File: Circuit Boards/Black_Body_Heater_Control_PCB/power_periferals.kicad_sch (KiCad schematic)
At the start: 17 parts, among them Q2 SI2310-TP, U2 INA181A2IDBVR, U3 LMR51420XFDDCR

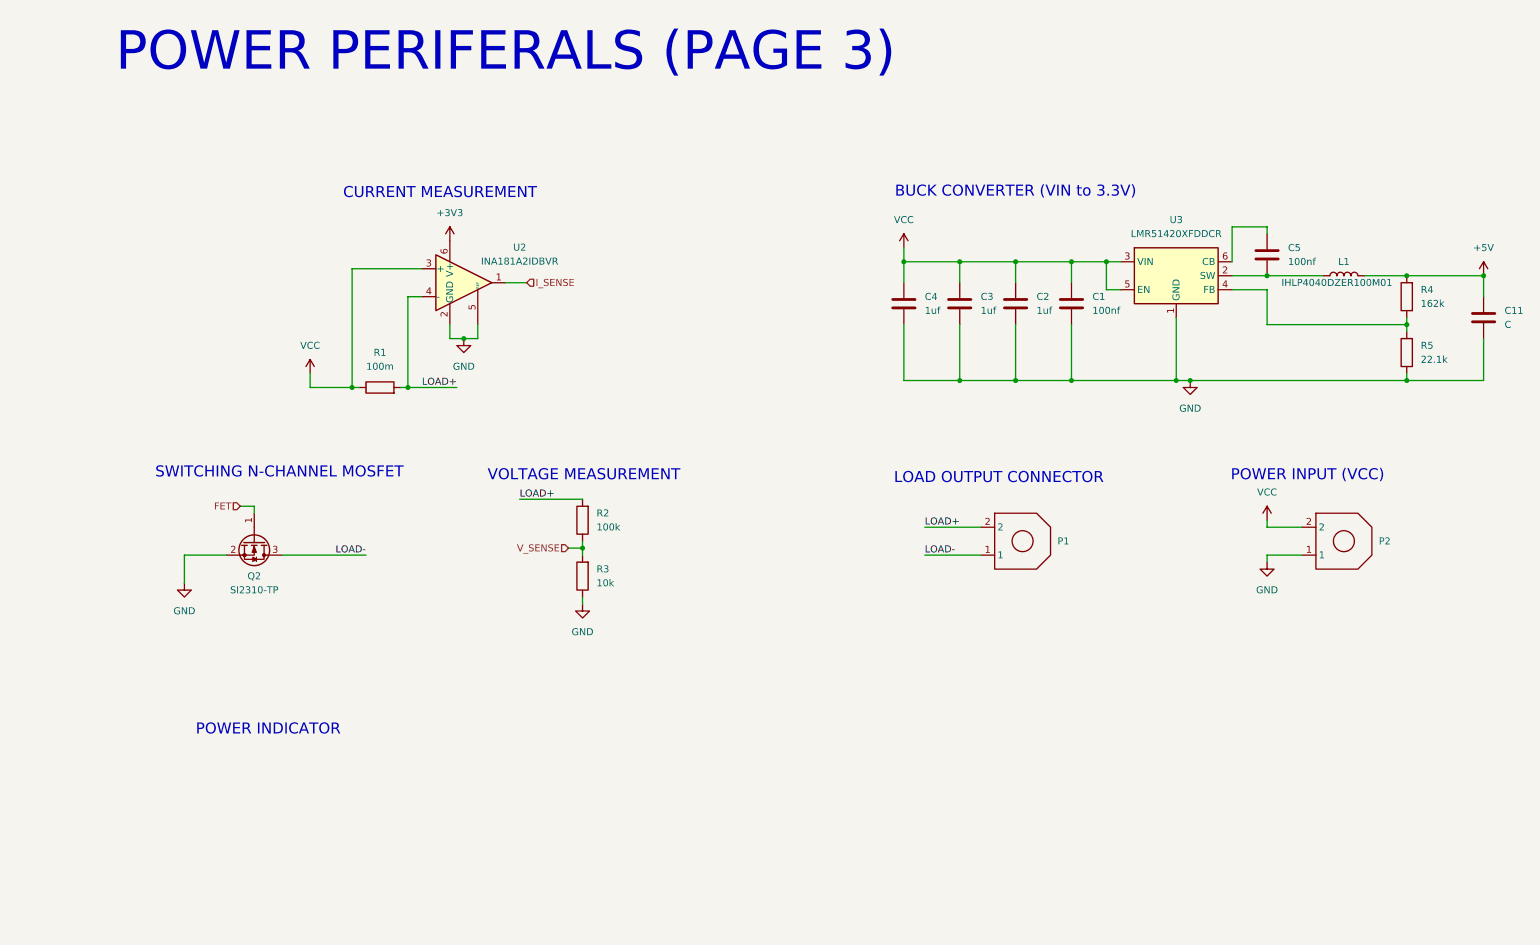
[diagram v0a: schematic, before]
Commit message: Heater PCB done (to review)
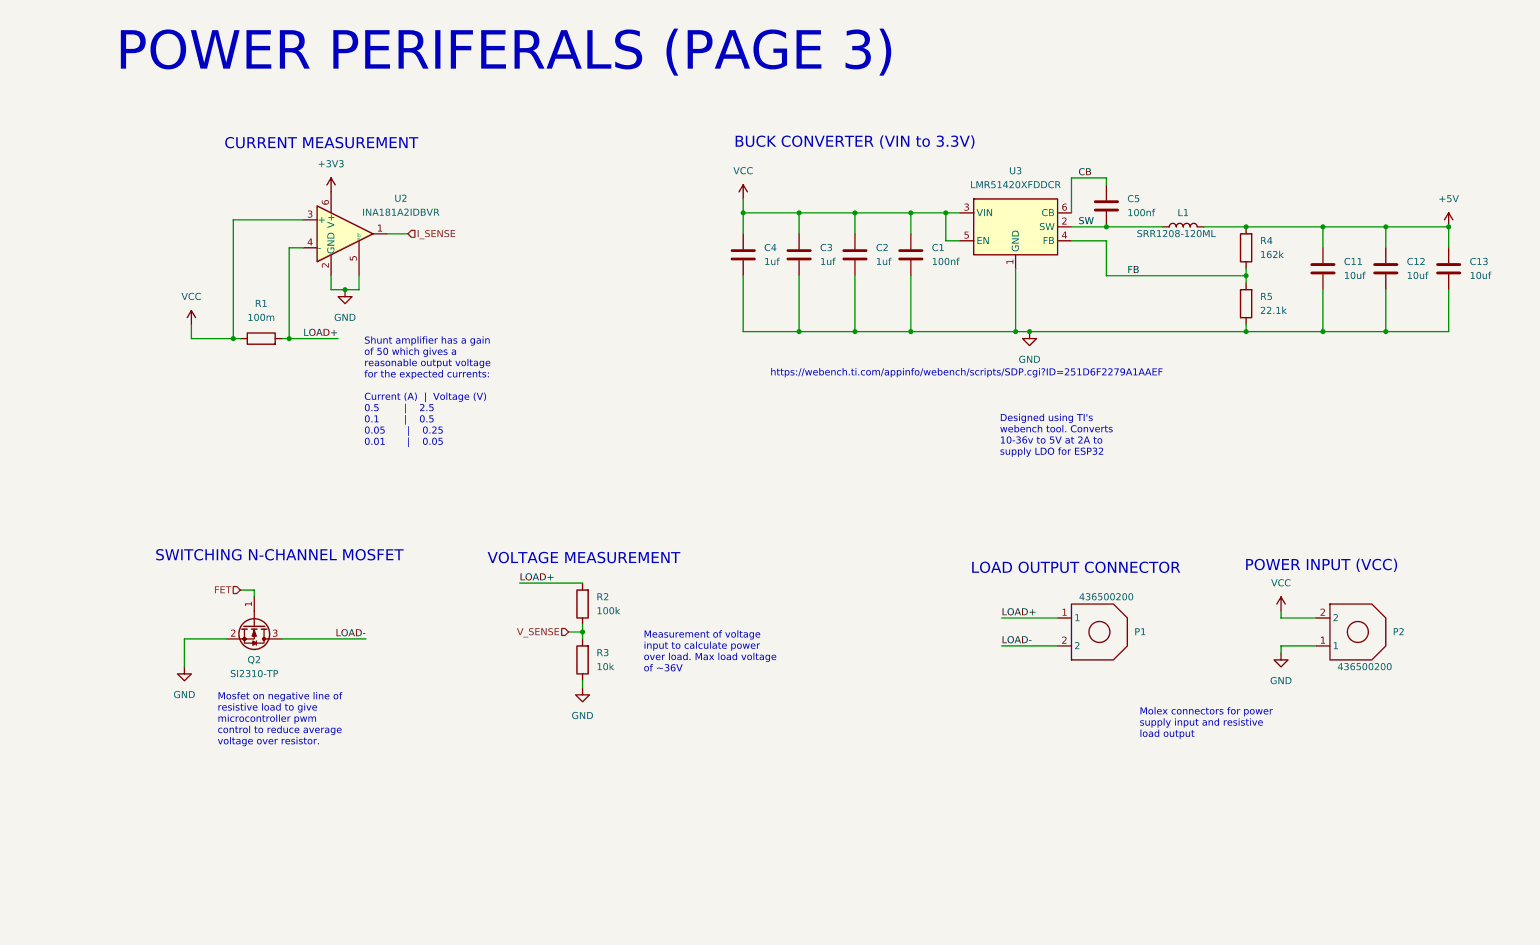
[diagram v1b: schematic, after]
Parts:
- added C12, C13: 10uf, Capacitor_SMD:C_0603_1608Metric, symbol Device:C
- C1, C2, C3, C4, C5: footprint (none) -> Capacitor_SMD:C_0603_1608Metric
- C11: value C -> 10uf; footprint (none) -> Capacitor_SMD:C_0603_1608Metric
- L1: value IHLP4040DZER100M01 -> SRR1208-120ML; footprint (none) -> -inductors:SRR1208
- P1, P2: value (none) -> 436500200
- R1, R2, R3, R4, R5: footprint (none) -> Resistor_SMD:R_0603_1608Metric
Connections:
- net +5V: now also C12.1, C13.1
- net GND: now also C12.2, C13.2
- net LOAD+: now also P1.1; no longer P1.2
- net LOAD-: now also P1.2; no longer P1.1
- net FB: now reaches R4.1, R5.2, U3.4 (FB)
- net CB: now reaches C5.1, U3.6 (CB)
- net SW: now reaches C5.2, L1.1, U3.2 (SW)
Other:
- note added: "https://webench.ti.com/appinfo/webench/scripts/SDP.cgi?ID=251D6F2279A1AAEF"
- note removed: "POWER INDICATOR"
- moved on the sheet: C1, C11, C2, C3, C4, C5, L1, P2, Q2, R1, R2, R3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

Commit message: Heater switched from pwm to vccs
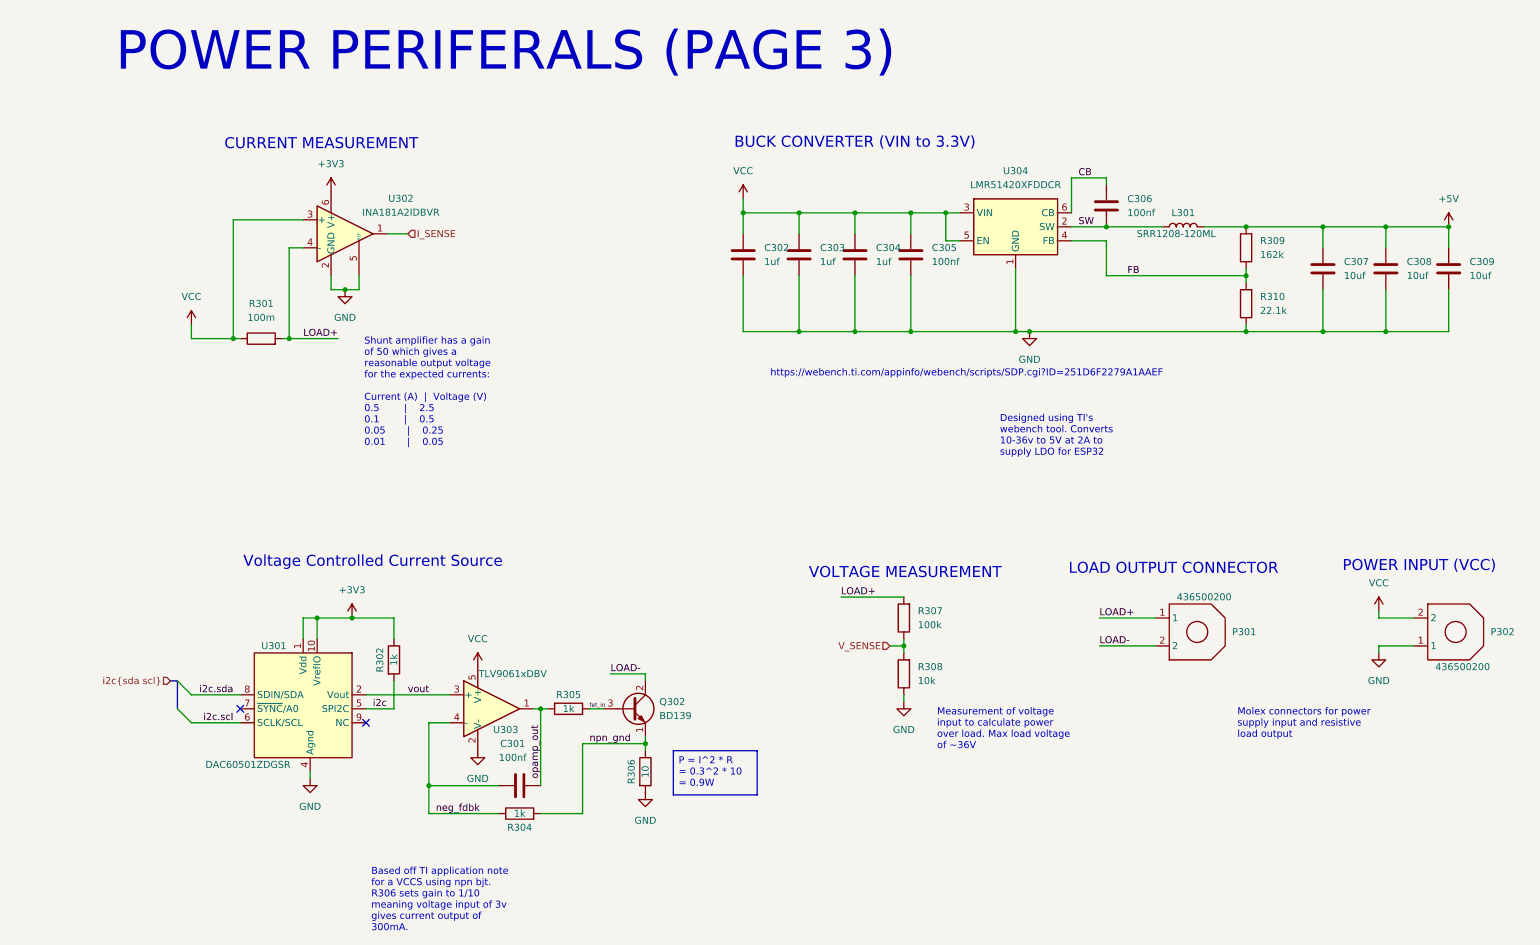
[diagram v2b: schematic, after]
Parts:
- removed Q2: SI2310-TP, Package_TO_SOT_SMD:SOT-23, symbol -fet:SI2310-TP
- added C301: 100nf, Capacitor_SMD:C_0603_1608Metric, symbol Device:C
- added Q302: BD139, Package_TO_SOT_THT:TO-126-3_Vertical, symbol Transistor_BJT:BD139
- added R302, R304, R305: 1k, Resistor_SMD:R_0603_1608Metric, symbol Device:R
- added R306: 10, Resistor_SMD:R_2512_6332Metric, symbol Device:R
- added U301: DAC60501ZDGSR, Package_SO:TSSOP-10_3x3mm_P0.5mm, symbol -dac:DAC60501ZDGSR
- added U303: TLV9061xDBV, Package_TO_SOT_SMD:SOT-23-5, symbol Amplifier_Operational:TLV9061xDBV
- R301: renamed from R1; footprint Resistor_SMD:R_0603_1608Metric -> Resistor_SMD:R_0805_2012Metric
- renumbered C4 to C302, C3 to C303, C2 to C304, C1 to C305, C5 to C306, C11 to C307, C12 to C308, C13 to C309, L1 to L301, P1 to P301, P2 to P302, R2 to R307, R3 to R308, R4 to R309, R5 to R310, U2 to U302, U3 to U304
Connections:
- net +3V3: now also R302.1, U301.1 (Vdd), U301.10 (VrefIO)
- net GND: now also R306.2, U301.4 (Agnd), U303.2 (V-)
- net LOAD-: now also Q302.2 (C)
- net VCC: now also U303.5 (V+)
- new net: U301.3 (NC), U301.9 (NC)
- new net fet_in: Q302.3 (B), R305.1
- new net i2c: R302.2, U301.5 (SPI2C)
- new net i2c.scl: U301.6 (SCLK/SCL)
- new net i2c.sda: U301.8 (SDIN/SDA)
- new net neg_fdbk: C301.1, R304.1, U303.4 (-)
- new net npn_gnd: Q302.1 (E), R304.2, R306.1
- new net opamp_out: C301.2, R305.2, U303.1
- new net vout: U301.2 (Vout), U303.3 (+)
- no-connect marks 0 -> 2
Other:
- note added: "Voltage Controlled Current Source"
- note removed: "SWITCHING N-CHANNEL MOSFET"
- moved on the sheet: P301, P302, R307, R308

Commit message: heater ready to order
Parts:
- added C310, C311, C312: 100nf, Capacitor_SMD:C_0603_1608Metric, symbol Device:C
- added R303, R311: 5.1k, Resistor_SMD:R_0603_1608Metric, symbol Device:R
- P301, P302: MPN (none) -> 436500200
- Q302: MPN (none) -> BD139
- R306: value 10 -> 5.1; MPN (none) -> CRM2512-FX-5R10ELF
- U301: MPN (none) -> DAC60501ZDGSR
- U302: MPN (none) -> INA181A2IDBVR
- U303: MPN (none) -> TLV9061xDBV
- U304: MPN (none) -> LMR51420XFDDCR
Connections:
- net +3V3: now also C310.2, C311.2, R303.1, R311.1; no longer U301.10 (VrefIO)
- net GND: now also C310.1, C311.1, C312.1
- net i2c.scl: now also R303.2
- net i2c.sda: now also R311.2
- new net vrefIO: C312.2, U301.10 (VrefIO)
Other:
- note added: "2.5V internal regulator"

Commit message: Designs finished - order placed
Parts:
- removed U303: TLV9061xDBV, Package_TO_SOT_SMD:SOT-23-5, symbol Amplifier_Operational:TLV9061xDBV
- added D301: SMAJ24A, Diode_SMD:D_SMA, symbol Diode:SMAJ24A
- added U305: LM358, Package_SO:SOIC-8_3.9x4.9mm_P1.27mm, symbol Amplifier_Operational:LM358
- C301, C305, C306, C310, C311, C312: MPN (none) -> CL10B104KB8NNNC
- C302, C303, C304: MPN (none) -> C0603C105K4RACTU
- C307, C308, C309: MPN (none) -> GRM188R6YA106MA73D
- L301: MPN (none) -> SRR1208-120ML
- R301: MPN (none) -> RCWE0805R100FKEA
- R302: value 1k -> 1.33k; MPN (none) -> ERA-3AEB1331V
- R303, R311: footprint Resistor_SMD:R_0603_1608Metric -> Resistor_SMD:R_0402_1005Metric; MPN (none) -> RT0402BRD075K1L
- R304, R305: value 1k -> 500; MPN (none) -> ERA-3AEB4990V
- R307: MPN (none) -> ERA-3AEB104V
- R308: MPN (none) -> ERA-3AEB103V
- R309: MPN (none) -> CRCW0603162KFKEA
- R310: value 22.1k -> 22.6k; MPN (none) -> ERA-3AEB2262V
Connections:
- net GND: now also D301.2 (A2), U305.4 (V-)
- net VCC: now also D301.1 (A1), U305.8 (V+)
- net neg_fdbk: now also U305.2 (-)
- net opamp_out: now also U305.1
- net vout: now also U305.3 (+)
- no-connect marks 2 -> 5
